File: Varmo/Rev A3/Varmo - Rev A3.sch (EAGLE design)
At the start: 110 parts, among them J1 22-05-7028-02, J2 22-05-7028-02, J3 22-05-7038-03, J4 22-05-7038-03, J5 22-05-7038-03, J6 22-05-7038-03, J7 22-05-7058-05, J9 22-05-7038-03, T1 MMBT2222AL, U1 LT1813, U2 SN74LVC2G17DBVR, U3 SN74LVC2G17DBVR, U4 PCA9665D, U5 90814-0210, U6 90814-0210, U8 M20DX256, X1 90814-0210, X2 90814-0210, X6 NC5MAV-SW, X7 90814-0210, X8 90814-0210

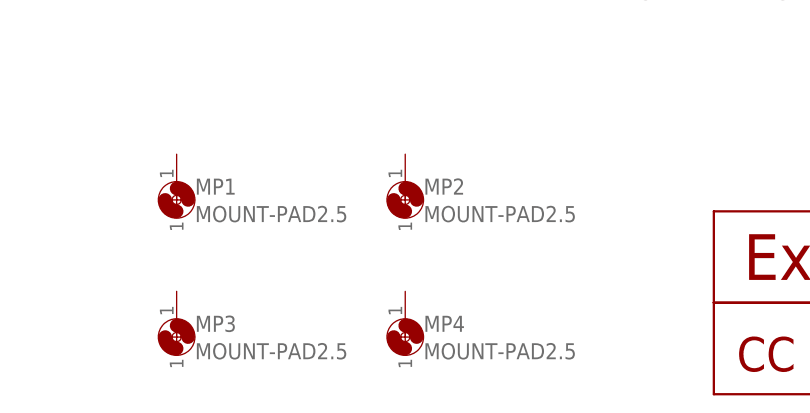
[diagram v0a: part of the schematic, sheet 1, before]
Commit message: Fix #7 : Replace M2.5 drill by M3
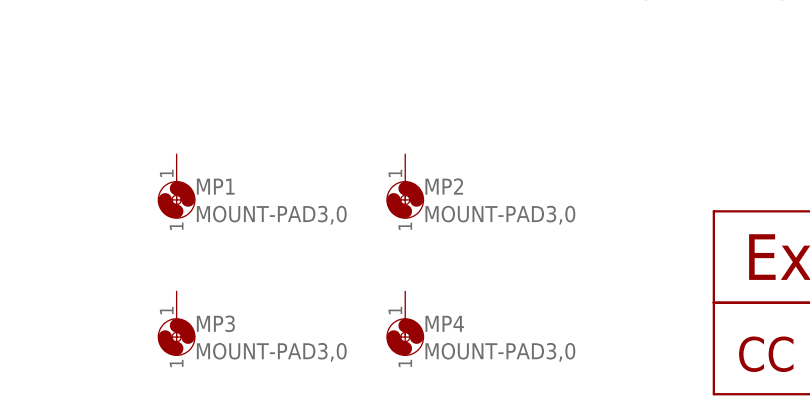
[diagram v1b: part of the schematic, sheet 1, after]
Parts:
- MP1, MP2, MP3, MP4, MP5, MP6, MP7, MP8: value MOUNT-PAD2.5 -> MOUNT-PAD3,0; device holes:MOUNT-PAD2.5 -> holes:MOUNT-PAD3,0
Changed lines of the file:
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@@
 <part name="+3V10" library="supply1" deviceset="+3V3" device=""/>
 <part name="+3V11" library="supply1" deviceset="+3V3" device=""/>
-<part name="MP1" library="holes" deviceset="MOUNT-PAD" device="2.5"/>
-<part name="MP2" library="holes" deviceset="MOUNT-PAD" device="2.5"/>
-<part name="MP3" library="holes" deviceset="MOUNT-PAD" device="2.5"/>
-<part name="MP4" library="holes" deviceset="MOUNT-PAD" device="2.5"/>
+<part name="MP1" library="holes" deviceset="MOUNT-PAD" device="3,0" value="MOUNT-PAD3,0"/>
+<part name="MP2" library="holes" deviceset="MOUNT-PAD" device="3,0" value="MOUNT-PAD3,0"/>
+<part name="MP3" library="holes" deviceset="MOUNT-PAD" device="3,0" value="MOUNT-PAD3,0"/>
+<part name="MP4" library="holes" deviceset="MOUNT-PAD" device="3,0" value="MOUNT-PAD3,0"/>
 <part name="J6" library="con-molex" deviceset="22-?-03" device="05-7038"/>
 <part name="J9" library="con-molex" deviceset="22-?-03" device="05-7038"/>
@@
 <part name="SUPPLY42" library="supply2" deviceset="GND1" device=""/>
 <part name="SUPPLY44" library="supply2" deviceset="GND1" device=""/>
-<part name="MP5" library="holes" deviceset="MOUNT-PAD" device="2.5"/>
-<part name="MP6" library="holes" deviceset="MOUNT-PAD" device="2.5"/>
-<part name="MP7" library="holes" deviceset="MOUNT-PAD" device="2.5"/>
-<part name="MP8" library="holes" deviceset="MOUNT-PAD" device="2.5"/>
+<part name="MP5" library="holes" deviceset="MOUNT-PAD" device="3,0" value="MOUNT-PAD3,0"/>
+<part name="MP6" library="holes" deviceset="MOUNT-PAD" device="3,0" value="MOUNT-PAD3,0"/>
+<part name="MP7" library="holes" deviceset="MOUNT-PAD" device="3,0" value="MOUNT-PAD3,0"/>
+<part name="MP8" library="holes" deviceset="MOUNT-PAD" device="3,0" value="MOUNT-PAD3,0"/>
 <part name="U8" library="custom" deviceset="M20DX256" device=""/>
 <part name="SUPPLY46" library="supply2" deviceset="+5V/1" device=""/>

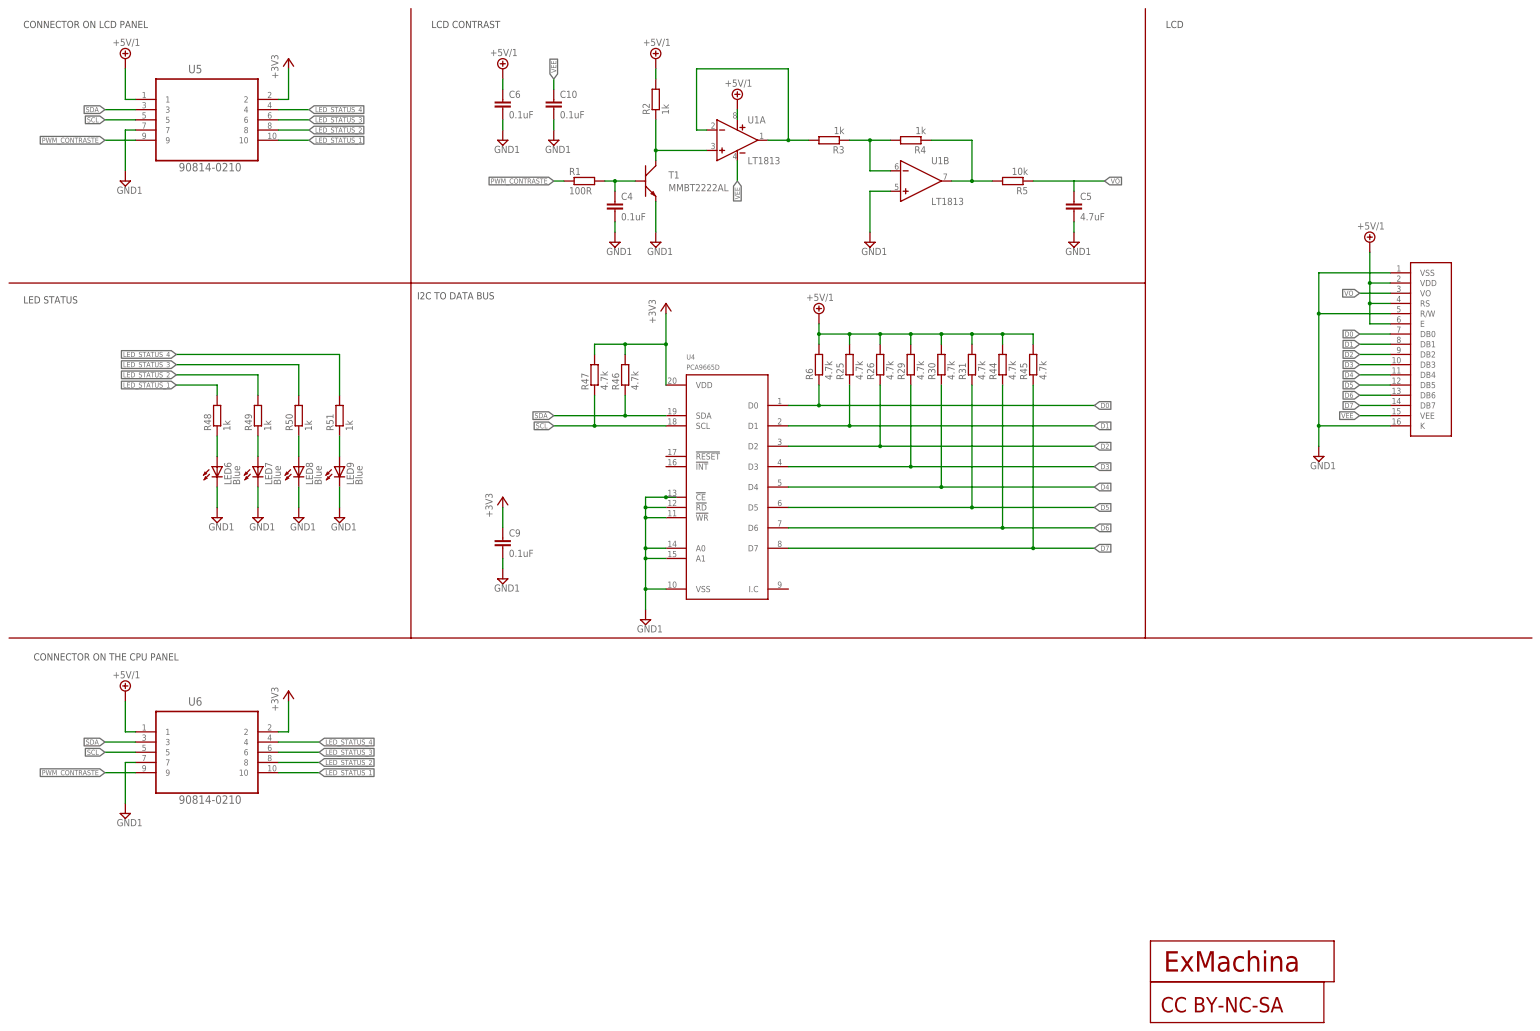
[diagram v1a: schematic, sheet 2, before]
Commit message: REplace the old version of LCD Screen by the new one
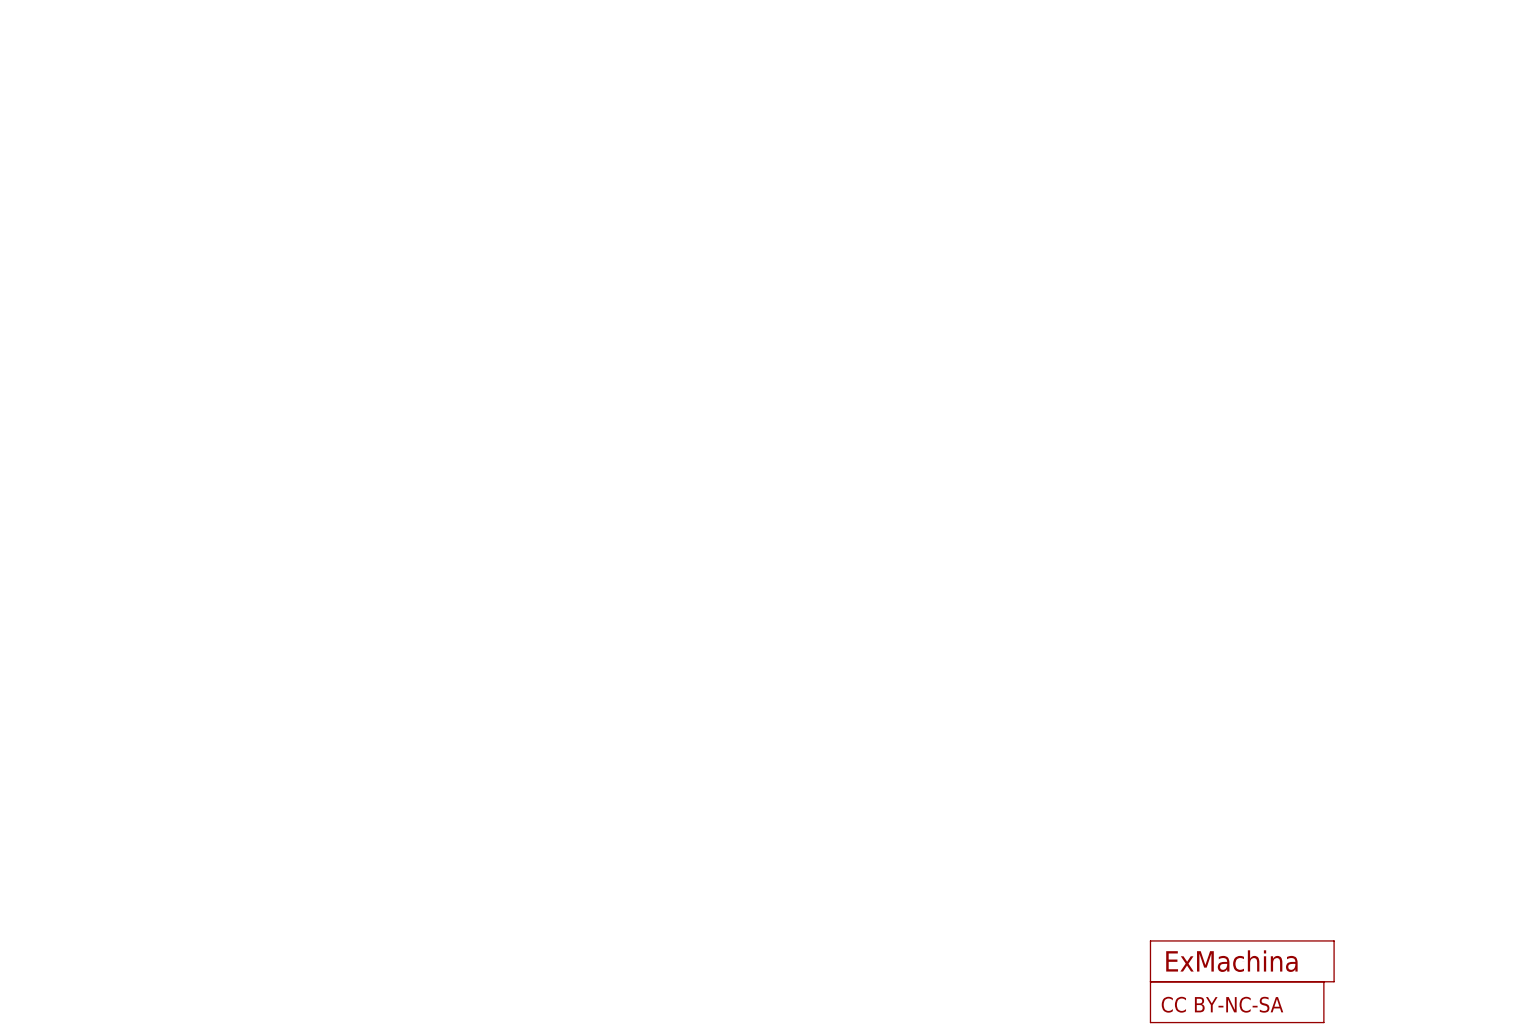
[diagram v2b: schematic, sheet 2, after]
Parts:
- removed C10, C4, C6, C9: 0.1uF, rcl:C-EUC0603
- removed C5: 4.7uF, rcl:C-EUC0603
- removed LCD1: MC41605A12W, midas:MC41605A12W
- removed LED6, LED7, LED8, LED9: Blue, led:LEDCHIP-LED0603
- removed R1: 100R, rcl:R-EU_R0603
- removed R2, R3, R4, R48, R49, R50, R51: 1k, rcl:R-EU_R0603
- removed R25, R26, R29, R30, R31, R44, R45, R46, R47, R6: 4.7k, rcl:R-EU_R0603
- removed R5: 10k, rcl:R-EU_R0603
- removed T1: MMBT2222AL, transistor:MMBT2222AL
- removed U1: LT1813, lineartechnology:LT1813
- removed U4: PCA9665D, NXP:PCA9665D
- removed U5, U6: 90814-0210, Molex_By_element14_Batch_1:90814-0210
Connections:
- removed net D0: LCD1.DB0, R6.1, U4.D0
- removed net D1: LCD1.DB1, R25.1, U4.D1
- removed net D2: LCD1.DB2, R26.1, U4.D2
- removed net D3: LCD1.DB3, R29.1, U4.D3
- removed net D4: LCD1.DB4, R30.1, U4.D4
- removed net D5: LCD1.DB5, R31.1, U4.D5
- removed net D6: LCD1.DB6, R44.1, U4.D6
- removed net D7: LCD1.DB7, R45.1, U4.D7
- removed net N$14: R3.1, R4.2, U1B.IN-
- removed net N$17: R4.1, R5.2, U1B.OUT
- removed net N$2: C4.1, R1.2, T1.B
- removed net N$22: LED7.A, R49.1
- removed net N$24: LED8.A, R50.1
- removed net N$29: LED9.A, R51.1
- removed net N$3: R2.1, T1.C, U1A.IN+
- removed net N$4: LED6.A, R48.1
- removed net N$5: R3.2, U1A.IN-, U1A.OUT
- removed net VEE: C10.1, LCD1.VEE, U1A.V-
- removed net VO: C5.1, LCD1.VO, R5.1
- net +3V3: no longer C9.1, R46.2, R47.2, U4.VDD, U5.2, U6.2
- net +5V/1: no longer C6.1, LCD1.E, LCD1.RS, LCD1.VDD, R2.2, R25.2, R26.2, R29.2, R30.2, R31.2, R44.2, R45.2, R6.2, U1A.V+, U5.1, U6.1
- net GND1: no longer C10.2, C4.2, C5.2, C6.2, C9.2, LCD1.K, LCD1.R/W, LCD1.VSS, LED6.C, LED7.C, LED8.C, LED9.C, T1.E, U1B.IN+, U4.!CE, U4.!RD, U4.!WR, U4.A0, U4.A1, U4.VSS, U5.7, U6.7
- net LED_STATUS_1: no longer R48.2, U5.10, U6.10
- net LED_STATUS_2: no longer R49.2, U5.8, U6.8
- net LED_STATUS_3: no longer R50.2, U5.6, U6.6
- net LED_STATUS_4: no longer R51.2, U5.4, U6.4
- net PWM_CONTRASTE: no longer R1.1, U5.9, U6.9
- net SCL: no longer R47.1, U4.SCL, U5.5, U6.5
- net SDA: no longer R46.1, U4.SDA, U5.3, U6.3
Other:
- note removed: "CONNECTOR ON LCD PANEL"
- note removed: "CONNECTOR ON THE CPU PANEL"
- note removed: "I2C TO DATA BUS"
- note removed: "LCD"
- note removed: "LCD CONTRAST"
- note removed: "LED STATUS"

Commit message: Replace LED postiiton
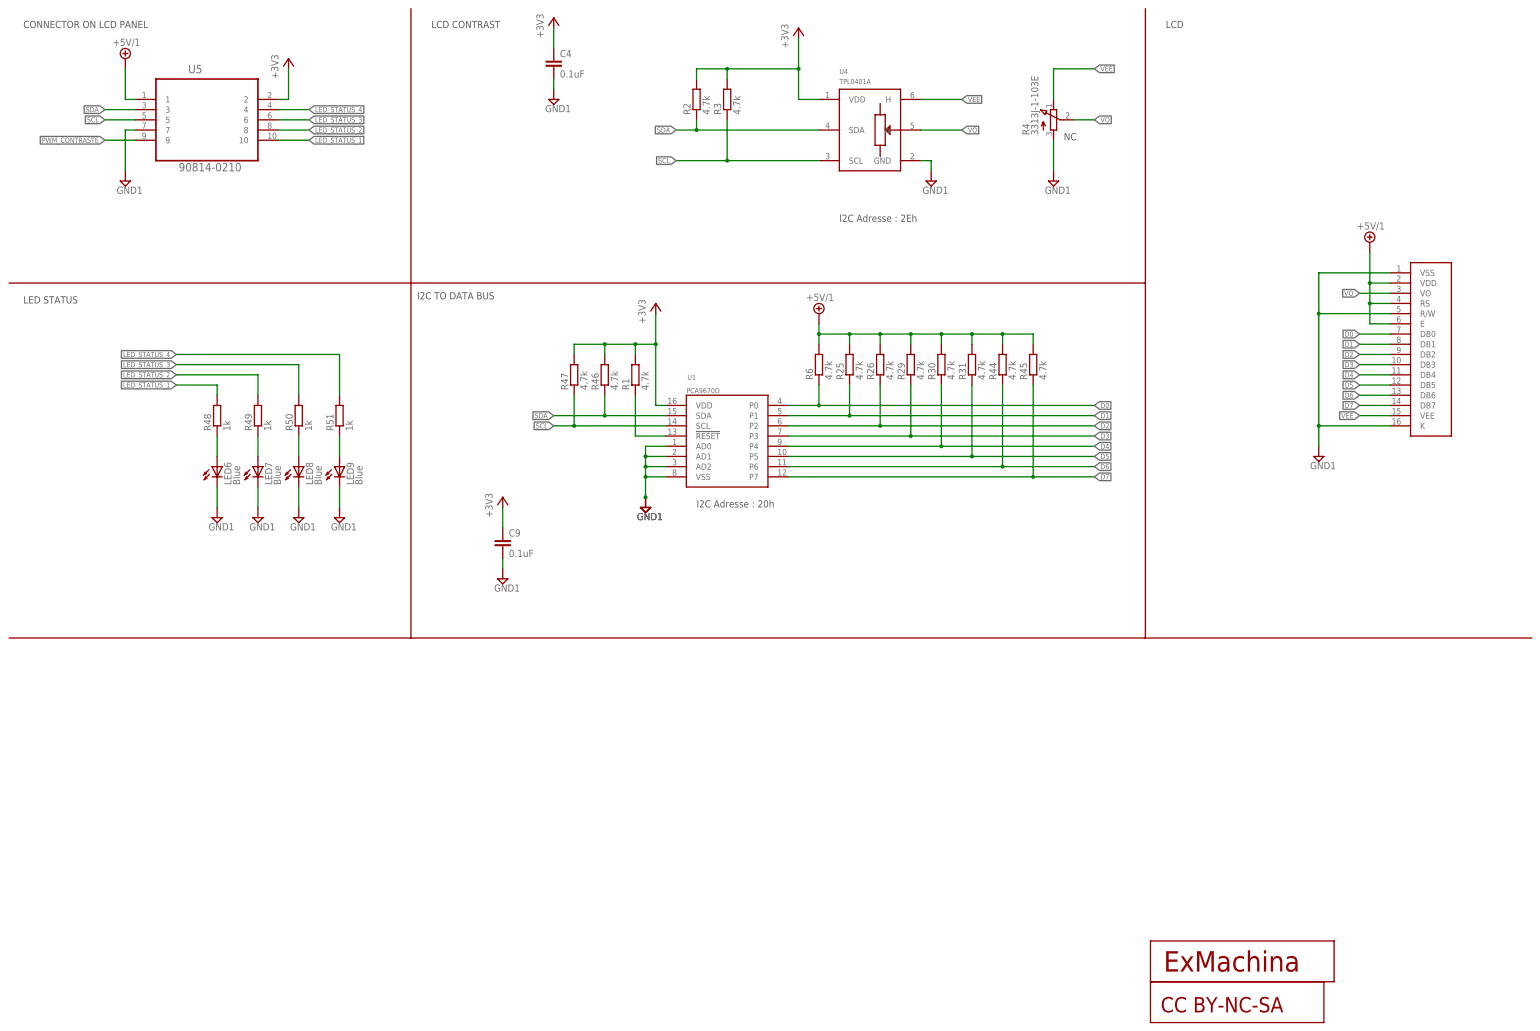
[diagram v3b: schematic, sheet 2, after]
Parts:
- added C4, C9: 0.1uF, rcl:C-EUC0603
- added LCD1: MC41605A12W, midas:MC41605A12W
- added LED6, LED7, LED8, LED9: Blue, led:LEDCHIP-LED0603
- added R1, R2, R25, R26, R29, R3, R30, R31, R44, R45, R46, R47, R6: 4.7k, rcl:R-EU_R0603
- added R4: 3313J-1-103E, pot:3313J-1-103E
- added R48, R49, R50, R51: 1k, rcl:R-EU_R0603
- added U1: PCA9670D, NXP:PCA9670D
- added U4: TPL0401A, ti:TPL0401A
- added U5: 90814-0210, Molex_By_element14_Batch_1:90814-0210
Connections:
- new net D0: LCD1.DB0, R6.1, U1.P0
- new net D1: LCD1.DB1, R25.1, U1.P1
- new net D2: LCD1.DB2, R26.1, U1.P2
- new net D3: LCD1.DB3, R29.1, U1.P3
- new net D4: LCD1.DB4, R30.1, U1.P4
- new net D5: LCD1.DB5, R31.1, U1.P5
- new net D6: LCD1.DB6, R44.1, U1.P6
- new net D7: LCD1.DB7, R45.1, U1.P7
- new net N$2: R1.1, U1.!RESET
- new net N$22: LED7.A, R49.1
- new net N$24: LED8.A, R50.1
- new net N$29: LED9.A, R51.1
- new net N$4: LED6.A, R48.1
- new net VEE: LCD1.VEE, R4.E, U4.H
- new net VO: LCD1.VO, R4.S, U4.W
- net +3V3: now also C4.1, C9.1, R1.2, R2.2, R3.2, R46.2, R47.2, U1.VDD, U4.VDD, U5.2
- net +5V/1: now also LCD1.E, LCD1.RS, LCD1.VDD, R25.2, R26.2, R29.2, R30.2, R31.2, R44.2, R45.2, R6.2, U5.1
- net GND1: now also C4.2, C9.2, LCD1.K, LCD1.R/W, LCD1.VSS, LED6.C, LED7.C, LED8.C, LED9.C, R4.A, U1.AD0, U1.AD1, U1.AD2, U1.VSS, U4.GND, U5.7
- net LED_STATUS_1: now also R48.2, U5.10
- net LED_STATUS_2: now also R49.2, U5.8
- net LED_STATUS_3: now also R50.2, U5.6
- net LED_STATUS_4: now also R51.2, U5.4
- net PWM_CONTRASTE: now also U5.9
- net SCL: now also R3.1, R47.1, U1.SCL, U4.SCL, U5.5
- net SDA: now also R2.1, R46.1, U1.SDA, U4.SDA, U5.3
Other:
- note added: "CONNECTOR ON LCD PANEL"
- note added: "I2C Adresse : 20h"
- note added: "I2C Adresse : 2Eh"
- note added: "I2C TO DATA BUS"
- note added: "LCD"
- note added: "LCD CONTRAST"
- note added: "LED STATUS"
- note added: "NC"

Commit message: Fix #9 : Change PCA9670D to PCA9671D and route the LCD Board
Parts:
- removed U$7: EXMACHINA-LOGO-NAME, exmachina:EXMACHINA-LOGO-NAME
- added R28, R32, R5: 4.7k, rcl:R-EU_R0603
- added U$10: PCA9671D, NXP:PCA9671D
- U$2: value EC20AE -> EC20A1824401; device encoder:EC20AE -> encoder:EC20A1824401
- U1: value PCA9670D -> 90814-0210; device NXP:PCA9670D -> Molex_By_element14_Batch_1:90814-0210
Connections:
- new net E: LCD1.E, R5.1, U$10.P10
- new net R/W: LCD1.R/W, R28.1, U$10.P11
- new net RS: LCD1.RS, R32.1, U$10.P12
- net +3V3: now also U$10.VDD, U1.2; no longer U1.VDD
- net +5V/1: now also R28.2, R32.2, R5.2, U1.1; no longer LCD1.E, LCD1.RS
- net D0: now also U$10.P00; no longer U1.P0
- net D1: now also U$10.P01; no longer U1.P1
- net D2: now also U$10.P02; no longer U1.P2
- net D3: now also U$10.P03; no longer U1.P3
- net D4: now also U$10.P04; no longer U1.P4
- net D5: now also U$10.P05; no longer U1.P5
- net D6: now also U$10.P06; no longer U1.P6
- net D7: now also U$10.P07; no longer U1.P7
- net GND1: now also U$10.AD0, U$10.AD1, U$10.AD2, U$10.VSS, U1.7; no longer LCD1.R/W, U1.AD0, U1.AD1, U1.AD2, U1.VSS
- net LED_STATUS_1: now also U1.10
- net LED_STATUS_2: now also U1.8
- net LED_STATUS_3: now also U1.6
- net LED_STATUS_4: now also U1.4
- net N$2: now also U$10.!RESET; no longer U1.!RESET
- net PWM_CONTRASTE: now also U1.9; no longer U5.9, U8.PTA12
- net SCL: now also U$10.SCL, U1.5; no longer U1.SCL
- net SDA: now also U$10.SDA, U1.3; no longer U1.SDA
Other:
- note added: "CONNECTOR ON MCU PLANE"
- note added: "I2C Adresse : 40h"
- note added: "I2C TO LCD DATA BUS"
- note removed: "I2C Adresse : 20h"
- note removed: "I2C TO DATA BUS"
- moved on the sheet: R1, R46, R47

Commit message: Fix #8: Add filter and shmitt trigger to encoder inputs.
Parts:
- added C10, C17, C18, C19, C20, C21, C22, C23, C5, C6: 0.1uF, rcl:C-EUC0603
- added R37, R38, R39, R52, R55, R56, R57: 1k, rcl:R-EU_R0603
- added U6: SN74LVC3G17DCTR, ti:SN74LVC3G17DCTR
- added U7, U9: SN74LVC2G17DBVR, ti:SN74LVC2G17DBVR
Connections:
- new net DIR_A_MCU: U7.1Y, U8.PTC10
- new net DIR_B_MCU: U7.2Y, U8.PTC11
- new net DIR_C_MCU: U8.PTD0, U9.1Y
- new net DIR_D_MCU: U8.PTD1, U9.2Y
- new net ENCODER_A_MCU: U6.1A, U8.PTC8
- new net ENCODER_B_MCU: U6.2A, U8.PTC7
- new net N$17: C10.1, R39.2, U7.1A
- new net N$30: C17.1, R52.2, U7.2A
- new net N$31: C5.1, R37.2, U9.1A
- new net N$32: C6.1, R38.2, U9.2A
- new net N$40: C20.1, R55.2, U6.1Y
- new net N$41: C21.1, R56.2, U6.2Y
- new net N$42: C22.1, R57.2, U6.3Y
- new net PUSH_MCU: U6.3A, U8.PTC9
- net +3V3: now also C18.1, C19.1, C23.1, U6.VCC, U7.VCC, U9.VCC
- net DIR_A: now also R39.1; no longer U8.PTC10
- net DIR_B: now also R52.1; no longer U8.PTC11
- net DIR_C: now also R37.1; no longer U8.PTD0
- net DIR_D: now also R38.1; no longer U8.PTD1
- net ENCODER_A: now also R55.1; no longer U8.PTC8
- net ENCODER_B: now also R56.1; no longer U8.PTC7
- net GND1: now also C10.2, C17.2, C18.2, C19.2, C20.2, C21.2, C22.2, C23.2, C5.2, C6.2, U6.GND, U7.GND, U9.GND
- net PUSH: now also R57.1; no longer U8.PTC9
